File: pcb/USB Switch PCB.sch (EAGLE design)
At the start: 14 parts, among them Q1 2N7002P, Q2 2N7002P, U1 D1MINI, X1 UE27-USBA

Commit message: Some more PCB work.
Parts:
- added S1: SWITCH, USB Switch PCB:SWITCH
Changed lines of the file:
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@@
 <part name="GND2" library="supply1" library_urn="urn:adsk.eagle:library:371" deviceset="GND" device=""/>
 <part name="X1" library="USB Switch PCB" deviceset="UE27-USBA" device=""/>
+<part name="S1" library="USB Switch PCB" deviceset="SWITCH" device=""/>
 </parts>
 <sheets>
@@
 <instance part="GND2" gate="1" x="-53.34" y="17.78"/>
 <instance part="X1" gate="G$1" x="-27.94" y="66.04"/>
+<instance part="S1" gate="G$1" x="17.78" y="76.2"/>
 </instances>
 <busses>

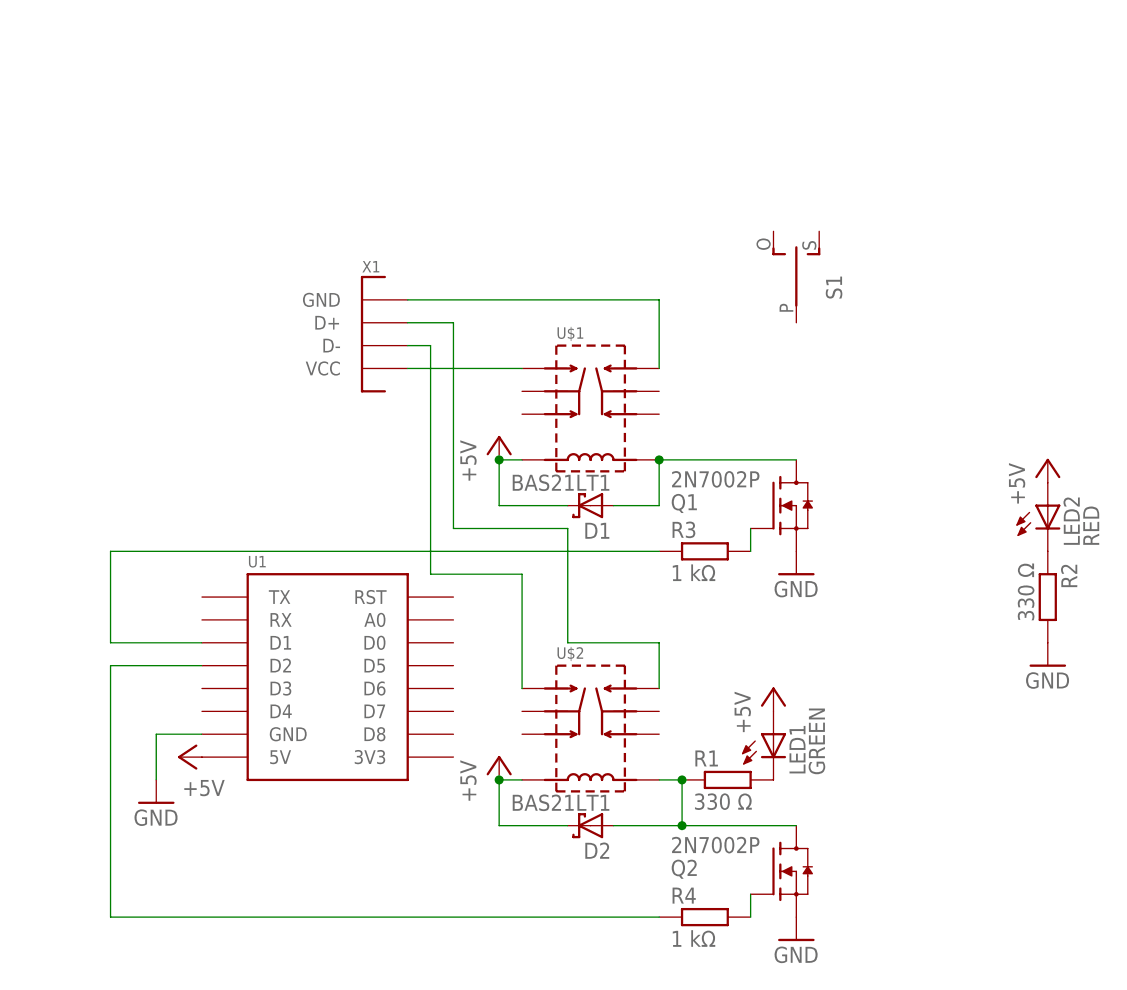
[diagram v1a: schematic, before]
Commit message: Added micro usb port.
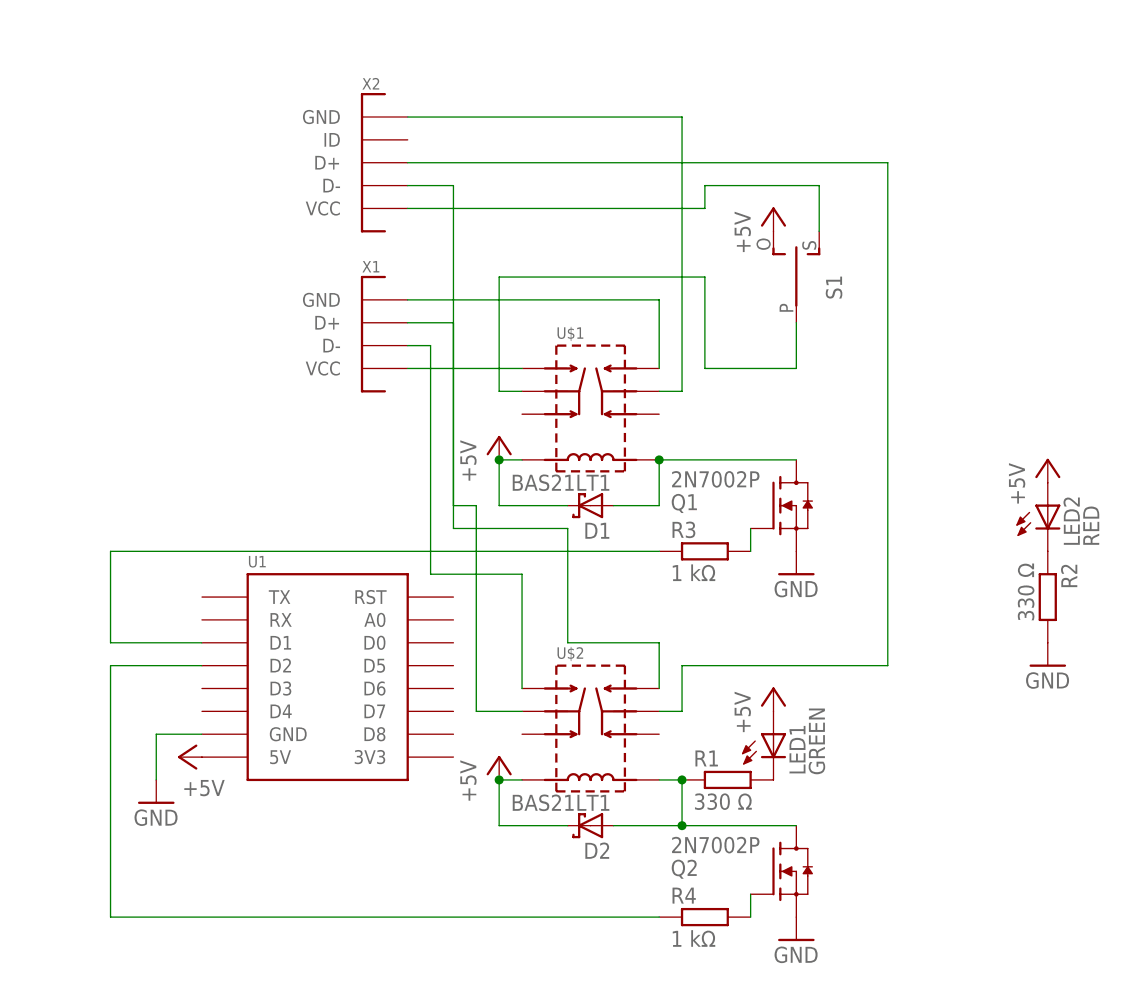
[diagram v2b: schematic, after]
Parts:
- added X2: HLP511-USBMICROB, USB Switch PCB:HLP511-USBMICROB
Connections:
- new net N$13: U$1.C2, X2.GND
- new net N$14: U$2.C2, X2.D+
- new net N$15: U$2.C1, X2.D-
- new net N$16: S1.P, U$1.C1
- new net N$17: S1.S, X2.VCC
- net +5V: now also S1.O
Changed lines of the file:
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@@
 <part name="X1" library="USB Switch PCB" deviceset="UE27-USBA" device=""/>
 <part name="S1" library="USB Switch PCB" deviceset="SWITCH" device=""/>
+<part name="X2" library="USB Switch PCB" deviceset="HLP511-USBMICROB" device=""/>
+<part name="P+4" library="supply1" library_urn="urn:adsk.eagle:library:371" deviceset="+5V" device=""/>
 </parts>
 <sheets>
@@
 <instance part="X1" gate="G$1" x="-27.94" y="66.04"/>
 <instance part="S1" gate="G$1" x="17.78" y="76.2"/>
+<instance part="X2" gate="G$1" x="-27.94" y="83.82"/>
+<instance part="P+4" gate="1" x="15.24" y="83.82"/>
 </instances>
 <busses>
@@
 <pinref part="U1" gate="G$1" pin="5V"/>
 <pinref part="P+3" gate="1" pin="+5V"/>
+</segment>
+<segment>
+<pinref part="S1" gate="G$1" pin="O"/>
+<pinref part="P+4" gate="1" pin="+5V"/>
 </segment>
 </net>
@@
 </segment>
 </net>
+<net name="N$13" class="0">
+<segment>
+<pinref part="X2" gate="G$1" pin="GND"/>
+<wire x1="-25.4" y1="93.98" x2="5.08" y2="93.98" width="0.1524" layer="91"/>
+<wire x1="5.08" y1="93.98" x2="5.08" y2="63.5" width="0.1524" layer="91"/>
+<pinref part="U$1" gate="G$1" pin="C2"/>
+<wire x1="5.08" y1="63.5" x2="2.54" y2="63.5" width="0.1524" layer="91"/>
+</segment>
+</net>
+<net name="N$14" class="0">
+<segment>
+<pinref part="X2" gate="G$1" pin="D+"/>
+<wire x1="-25.4" y1="88.9" x2="27.94" y2="88.9" width="0.1524" layer="91"/>
+<wire x1="27.94" y1="88.9" x2="27.94" y2="33.02" width="0.1524" layer="91"/>
+<wire x1="27.94" y1="33.02" x2="5.08" y2="33.02" width="0.1524" layer="91"/>
+<wire x1="5.08" y1="33.02" x2="5.08" y2="27.94" width="0.1524" layer="91"/>
+<pinref part="U$2" gate="G$1" pin="C2"/>
+<wire x1="5.08" y1="27.94" x2="2.54" y2="27.94" width="0.1524" layer="91"/>
+</segment>
+</net>
+<net name="N$15" class="0">
+<segment>
+<pinref part="U$2" gate="G$1" pin="C1"/>
+<wire x1="-12.7" y1="27.94" x2="-17.78" y2="27.94" width="0.1524" layer="91"/>
+<wire x1="-17.78" y1="27.94" x2="-17.78" y2="50.8" width="0.1524" layer="91"/>
+<wire x1="-17.78" y1="50.8" x2="-20.32" y2="50.8" width="0.1524" layer="91"/>
+<wire x1="-20.32" y1="50.8" x2="-20.32" y2="86.36" width="0.1524" layer="91"/>
+<pinref part="X2" gate="G$1" pin="D-"/>
+<wire x1="-20.32" y1="86.36" x2="-25.4" y2="86.36" width="0.1524" layer="91"/>
+</segment>
+</net>
+<net name="N$16" class="0">
+<segment>
+<pinref part="S1" gate="G$1" pin="P"/>
+<pinref part="U$1" gate="G$1" pin="C1"/>
+<wire x1="-12.7" y1="63.5" x2="-15.24" y2="63.5" width="0.1524" layer="91"/>
+<wire x1="-15.24" y1="63.5" x2="-15.24" y2="76.2" width="0.1524" layer="91"/>
+<wire x1="-15.24" y1="76.2" x2="7.62" y2="76.2" width="0.1524" layer="91"/>
+<wire x1="7.62" y1="76.2" x2="7.62" y2="66.04" width="0.1524" layer="91"/>
+<wire x1="7.62" y1="66.04" x2="17.78" y2="66.04" width="0.1524" layer="91"/>
+<wire x1="17.78" y1="66.04" x2="17.78" y2="71.12" width="0.1524" layer="91"/>
+</segment>
+</net>
+<net name="N$17" class="0">
+<segment>
+<pinref part="X2" gate="G$1" pin="VCC"/>
+<wire x1="-25.4" y1="83.82" x2="7.62" y2="83.82" width="0.1524" layer="91"/>
+<wire x1="7.62" y1="83.82" x2="7.62" y2="86.36" width="0.1524" layer="91"/>
+<pinref part="S1" gate="G$1" pin="S"/>
+<wire x1="7.62" y1="86.36" x2="20.32" y2="86.36" width="0.1524" layer="91"/>
+<wire x1="20.32" y1="86.36" x2="20.32" y2="81.28" width="0.1524" layer="91"/>
+</segment>
+</net>

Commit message: feat(usb-b): VCC supply fixed.
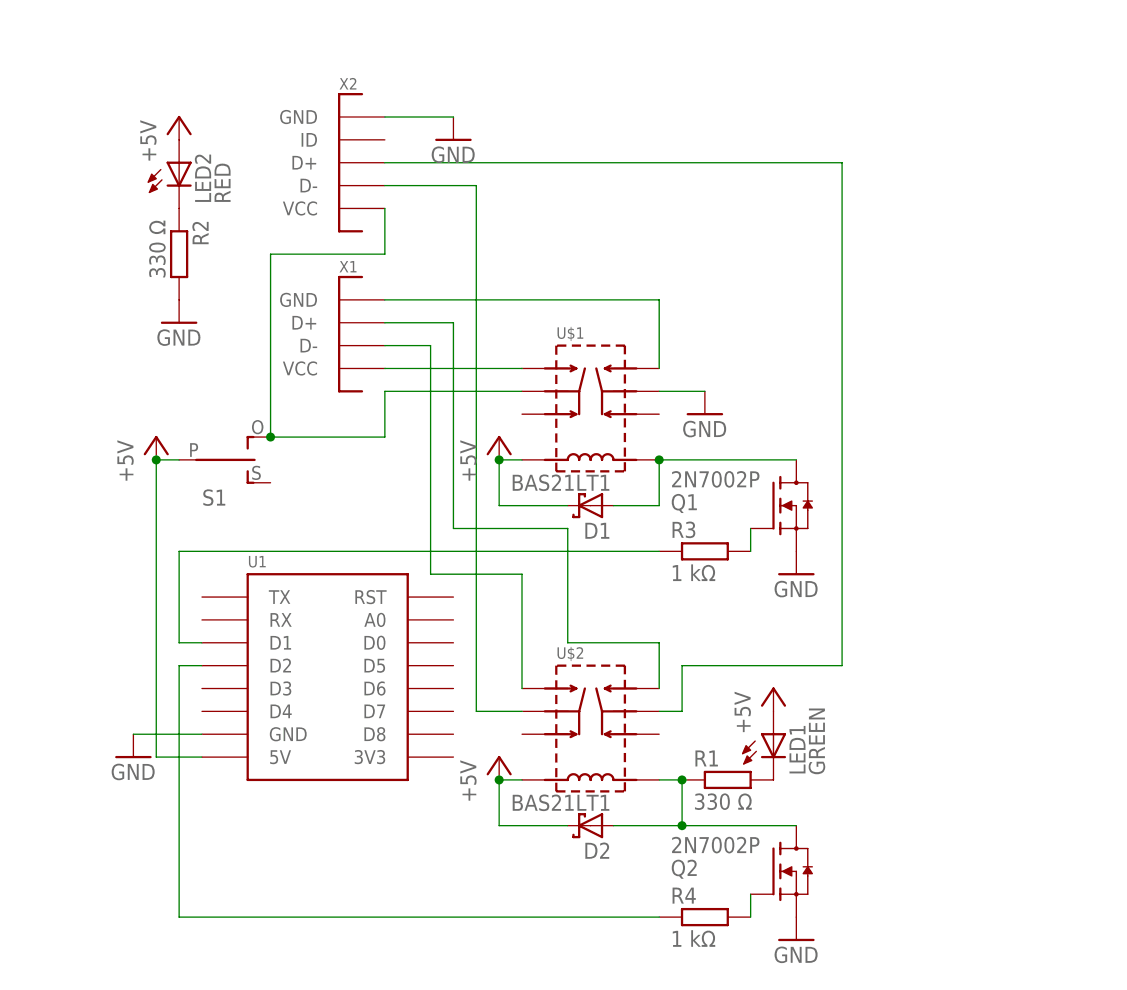
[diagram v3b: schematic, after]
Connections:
- removed net N$16: S1.P, U$1.C1
- removed net N$17: S1.S, X2.VCC
- net +5V: now also S1.P; no longer S1.O
- net GND: now also U$1.C2, X2.GND
- net N$13: now also S1.O, U$1.C1, X2.VCC; no longer U$1.C2, X2.GND
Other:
- moved on the sheet: LED2, R2, S1, X1, X2

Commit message: More work!
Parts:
- added UIN: (no value), con-lstb:MA05-1
- added UOUT: (no value), con-lstb:MA04-1
- X1: value UE27-USBA -> AMPHENOL-0001LF; device USB Switch PCB:UE27-USBA -> USB Switch PCB:AMPHENOL-0001LF
- X2: value HLP511-USBMICROB -> UE27-USBA; device USB Switch PCB:HLP511-USBMICROB -> USB Switch PCB:UE27-USBA
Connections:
- net N$5 renamed PWRON
- net N$7 renamed DATAON
- removed net N$10: U$1.A2, X1.GND
- removed net N$11: U$2.A1, X1.D-
- removed net N$12: U$2.A2, X1.D+
- removed net N$13: S1.O, U$1.C1, X2.VCC
- removed net N$14: U$2.C2, X2.D+
- removed net N$15: U$2.C1, X2.D-
- removed net N$9: U$1.A1, X1.VCC
- new net 5VESP: S1.S, U1.5V
- new net 5VUSB: S1.O, U$1.C1, UIN.1, X1.VCC
- new net D+: U$2.C2, UIN.3, X1.D+
- new net D+O: U$2.A2, UOUT.3, X2.D+
- new net D-: U$2.C1, UIN.2, X1.D-
- new net D-O: U$2.A1, UOUT.2, X2.D-
- new net GNDO: U$1.A2, UOUT.4, X2.GND
- new net N$16: UIN.4, X1.ID
- new net VCC0: U$1.A1, UOUT.1, X2.VCC
- net +5V: no longer U1.5V
- net GND: now also UIN.5, X1.GND; no longer X2.GND
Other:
- moved on the sheet: D2, LED1, LED2, Q2, R1, R2, R4, U$2
